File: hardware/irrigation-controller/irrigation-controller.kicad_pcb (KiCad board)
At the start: 2 copper layers, 0 parts

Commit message: Initial controller pcb footprint import
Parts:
- added C1: 100nF, Capacitor_SMD:C_0603_1608Metric, F.Cu at (190.5, 84.8)
- added C10: 15pF, Capacitor_SMD:C_0603_1608Metric, F.Cu at (259.0, 73.2)
- added C11: 8.2nF, Capacitor_SMD:C_0603_1608Metric, F.Cu at (239.0, 153.4)
- added C12: 8.2nF, Capacitor_SMD:C_0603_1608Metric, F.Cu at (260.9, 62.8)
- added C13: 2.7nF, Capacitor_SMD:C_0603_1608Metric, F.Cu at (257.6, 143.8)
- added C14: 1.5nF, Capacitor_SMD:C_0402_1005Metric, F.Cu at (263.1, 77.6)
- added C15: 100nF, Capacitor_SMD:C_0603_1608Metric, F.Cu at (253.7, 136.9)
- added C16: 100nF, Capacitor_SMD:C_0603_1608Metric, F.Cu at (256.8, 66.7)
- added C17: 10uF, Capacitor_SMD:C_1206_3216Metric, F.Cu at (242.1, 122.2)
- added C18: 10uF, Capacitor_SMD:C_1206_3216Metric, F.Cu at (271.0, 74.7)
- added C19: 10uF, Capacitor_SMD:C_1206_3216Metric, F.Cu at (227.6, 144.2)
- added C2: 100nF, Capacitor_SMD:C_0603_1608Metric, F.Cu at (174.6, 100.7)
- added C20: 10uF, Capacitor_SMD:C_1206_3216Metric, F.Cu at (253.7, 83.9)
- added C21: 10uF, Capacitor_SMD:C_1206_3216Metric, F.Cu at (236.7, 122.2)
- added C22: 10uF, Capacitor_SMD:C_1206_3216Metric, F.Cu at (261.4, 83.4)
- added C3: 100nF, Capacitor_SMD:C_0603_1608Metric, F.Cu at (149.9, 117.6)
- added C4: 100nF, Capacitor_SMD:C_0603_1608Metric, F.Cu at (145.8, 117.6)
- added C5: 22pF, Capacitor_SMD:C_0402_1005Metric, F.Cu at (182.0, 102.2)
- added C6: 22pF, Capacitor_SMD:C_0402_1005Metric, F.Cu at (167.9, 116.5)
- added C7: 10uF, Capacitor_SMD:C_1206_3216Metric, F.Cu at (221.5, 144.3)
- added C8: 10uF, Capacitor_SMD:C_1206_3216Metric, F.Cu at (250.4, 65.2)
- added C9: 27pF, Capacitor_SMD:C_0603_1608Metric, F.Cu at (250.7, 146.0)
- added D1: 1.1V 1A, Diode_SMD:D_SMA, F.Cu at (180.0, 85.9)
- added D2: 1.1V 1A, Diode_SMD:D_SMA, F.Cu at (147.9, 114.1)
- added D3: 550mV 1A, Diode_SMD:D_SMA, F.Cu at (247.7, 131.6)
- added D4: 550mV 1A, Diode_SMD:D_SMA, F.Cu at (265.1, 67.8)
- added J1: RS485, Connector_JST:JST_XH_B3B-XH-A_1x03_P2.50mm_Vertical, F.Cu at (118.7, 73.0)
- added J10: I2C_2, Connector_JST:JST_XH_B4B-XH-A_1x04_P2.50mm_Vertical, F.Cu at (97.1, 70.8)
- added J11: IO, Connector_PinHeader_2.54mm:PinHeader_2x04_P2.54mm_Vertical, F.Cu at (82.5, 84.3)
- added J12: RELAY_2, Connector_JST:JST_XH_B2B-XH-A_1x02_P2.50mm_Vertical, F.Cu at (110.9, 63.9)
- added J13: RELAY_3B, Connector_JST:JST_XH_B3B-XH-A_1x03_P2.50mm_Vertical, F.Cu at (89.8, 53.5)
- added J14: RELAY_4B, Connector_JST:JST_XH_B3B-XH-A_1x03_P2.50mm_Vertical, F.Cu at (127.7, 53.8)
- added J2: I2C_1, Connector_JST:JST_XH_B4B-XH-A_1x04_P2.50mm_Vertical, F.Cu at (97.5, 82.1)
- added J3: ATMEGA ICSP, Connector_PinHeader_2.54mm:PinHeader_2x03_P2.54mm_Vertical, F.Cu at (105.8, 51.9)
- added J4: ATMEGA UART, Connector_PinHeader_2.54mm:PinHeader_2x03_P2.54mm_Vertical, F.Cu at (111.7, 81.1)
- added J5: RF Module, Connector_PinSocket_2.54mm:PinSocket_1x07_P2.54mm_Vertical, F.Cu at (88.4, 62.2)
- added J6: PWR, Connector_JST:JST_XH_B2B-XH-A_1x02_P2.50mm_Vertical, F.Cu at (130.8, 72.7)
- added J7: RELAY_1, Connector_JST:JST_XH_B2B-XH-A_1x02_P2.50mm_Vertical, F.Cu at (195.0, 57.6)
- added J8: RELAY_3A, Connector_JST:JST_XH_B3B-XH-A_1x03_P2.50mm_Vertical, F.Cu at (125.5, 63.7)
- added J9: RELAY_4A, Connector_JST:JST_XH_B3B-XH-A_1x03_P2.50mm_Vertical, F.Cu at (115.7, 53.8)
- added K1: UA2-5NU, lib:Relay_DPDT_NEXEM_UA2_Pitch3.2mm, F.Cu at (145.1, 97.1)
- added K2: UA2-5NU, lib:Relay_DPDT_NEXEM_UA2_Pitch3.2mm, F.Cu at (170.0, 58.3)
- added L1: 4.7uH, Capacitor_THT:C_Radial_D5.0mm_H5.0mm_P2.00mm, F.Cu at (260.1, 110.5)
- added L2: 4.7uH, Capacitor_THT:C_Radial_D5.0mm_H5.0mm_P2.00mm, F.Cu at (242.5, 65.9)
- added Q1: MMBT3904, Package_TO_SOT_SMD:SOT-23, F.Cu at (167.9, 108.7)
- added Q2: MMBT3904, Package_TO_SOT_SMD:SOT-23, F.Cu at (184.8, 90.4)
- added Q3: 2N7002, Package_TO_SOT_SMD:SOT-23, F.Cu at (186.3, 85.9)
- added Q4: 2N7002, Package_TO_SOT_SMD:SOT-23, F.Cu at (177.6, 97.2)
- added Q5: 2N7002, Package_TO_SOT_SMD:SOT-23, F.Cu at (162.3, 112.1)
- added Q6: 2N7002, Package_TO_SOT_SMD:SOT-23, F.Cu at (170.3, 101.7)
- added R1: 2.2k, Resistor_SMD:R_0402_1005Metric, F.Cu at (129.0, 109.0)
- added R10: 10k, Resistor_SMD:R_0402_1005Metric, F.Cu at (133.3, 87.2)
- added R11: 10k, Resistor_SMD:R_0402_1005Metric, F.Cu at (185.2, 95.7)
- added R12: 120, Resistor_SMD:R_0603_1608Metric, F.Cu at (189.0, 89.9)
- added R13: 10k, Resistor_SMD:R_0402_1005Metric, F.Cu at (175.6, 107.4)
- added R14: 10k, Resistor_SMD:R_0402_1005Metric, F.Cu at (167.9, 114.5)
- added R15: 10k, Resistor_SMD:R_0402_1005Metric, F.Cu at (184.1, 98.2)
- added R16: 10k, Resistor_SMD:R_0402_1005Metric, F.Cu at (265.2, 149.4)
- added R17: 3k, Resistor_SMD:R_0603_1608Metric, F.Cu at (264.9, 144.3)
- added R18: 10k, Resistor_SMD:R_0402_1005Metric, F.Cu at (240.6, 74.4)
- added R19: 1.8k, Resistor_SMD:R_0603_1608Metric, F.Cu at (245.2, 78.4)
- added R2: 620, Resistor_SMD:R_0603_1608Metric, F.Cu at (166.5, 112.3)
- added R20: 10k, Resistor_SMD:R_0402_1005Metric, F.Cu at (170.0, 112.0)
- added R3: 620, Resistor_SMD:R_0603_1608Metric, F.Cu at (181.8, 95.9)
- added R4: 2.2k, Resistor_SMD:R_0402_1005Metric, F.Cu at (162.8, 117.9)
- added R5: 10k, Resistor_SMD:R_0402_1005Metric, F.Cu at (181.2, 98.2)
- added R6: 10k, Resistor_SMD:R_0402_1005Metric, F.Cu at (159.9, 117.9)
- added R7: 10k, Resistor_SMD:R_0402_1005Metric, F.Cu at (184.0, 93.7)
- added R8: 12k, Resistor_SMD:R_0603_1608Metric, F.Cu at (252.2, 150.4)
- added R9: 20k, Resistor_SMD:R_0603_1608Metric, F.Cu at (256.4, 78.7)
- added SW1: SPST, lib:SW_SPST_THT_5.0mm, F.Cu at (183.1, 58.3)
- added U1: AQY280EH, Package_DIP:DIP-4_W7.62mm, F.Cu at (157.3, 89.2)
- added U2: ATmega328P-AU, Package_QFP:TQFP-32_7x7mm_P0.8mm, F.Cu at (101.0, 108.5)
- added U3: AQY280EH, Package_DIP:DIP-4_W7.62mm, F.Cu at (125.2, 112.7)
- added U4: TPS54331DR, TPS54331DR:Texas_Instruments-TPS54331DR-Level_A, F.Cu at (242.3, 145.8)
- added U5: TPS54331DR, TPS54331DR:Texas_Instruments-TPS54331DR-Level_A, F.Cu at (249.8, 72.4)
- added U6: MAX485, Package_DIP:DIP-8_W7.62mm, F.Cu at (146.5, 85.4)
- added Y1: 8MHz, Crystal:Crystal_SMD_5032-2Pin_5.0x3.2mm, F.Cu at (127.2, 105.6)
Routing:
- added copper zone on B.Cu, net GND
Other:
- board outline added: 207.8 x 117.3 mm

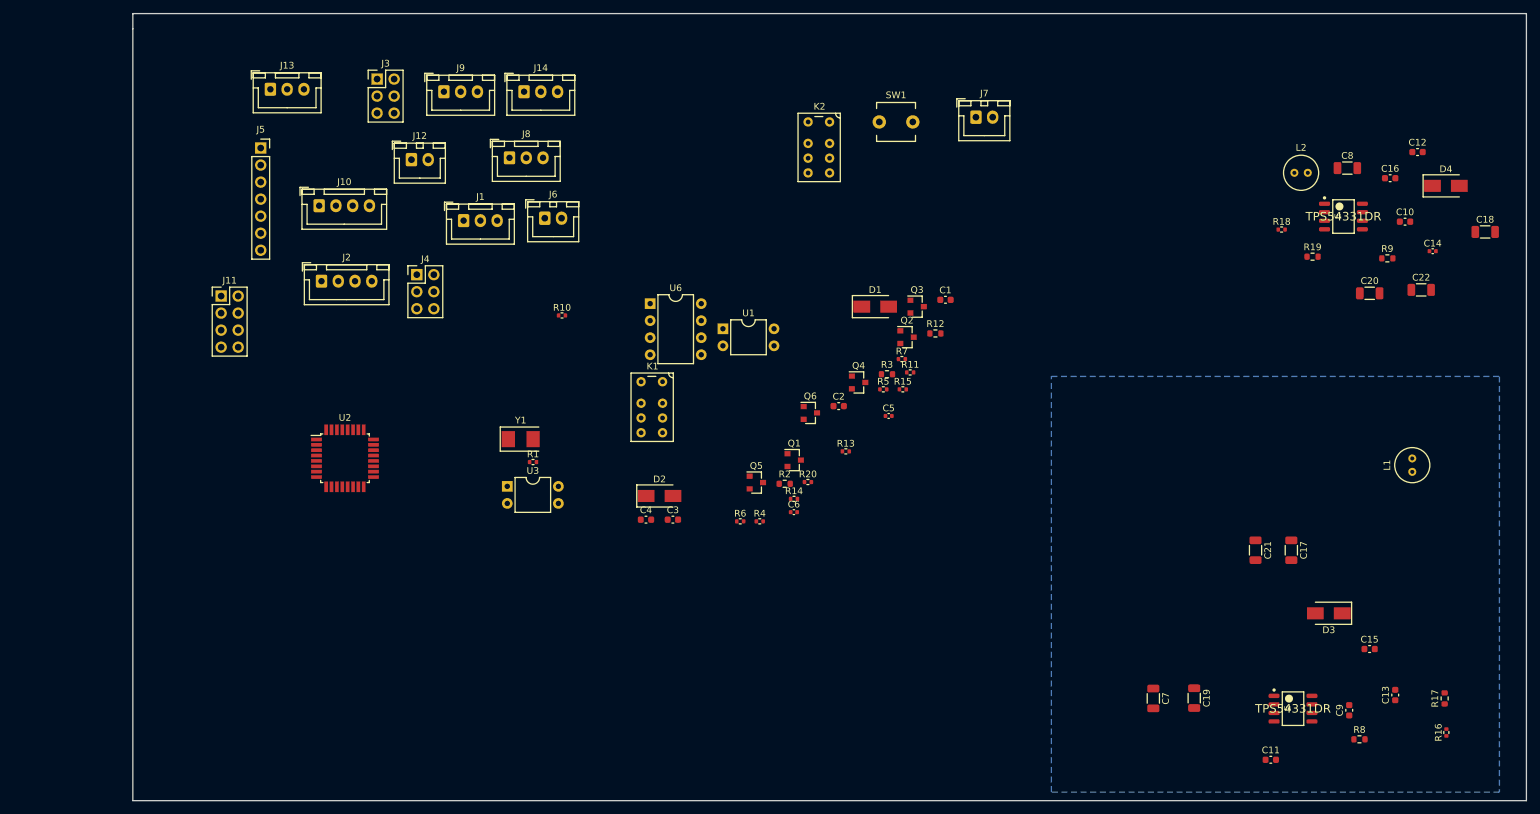
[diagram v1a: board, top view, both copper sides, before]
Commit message: Controller board layout wip
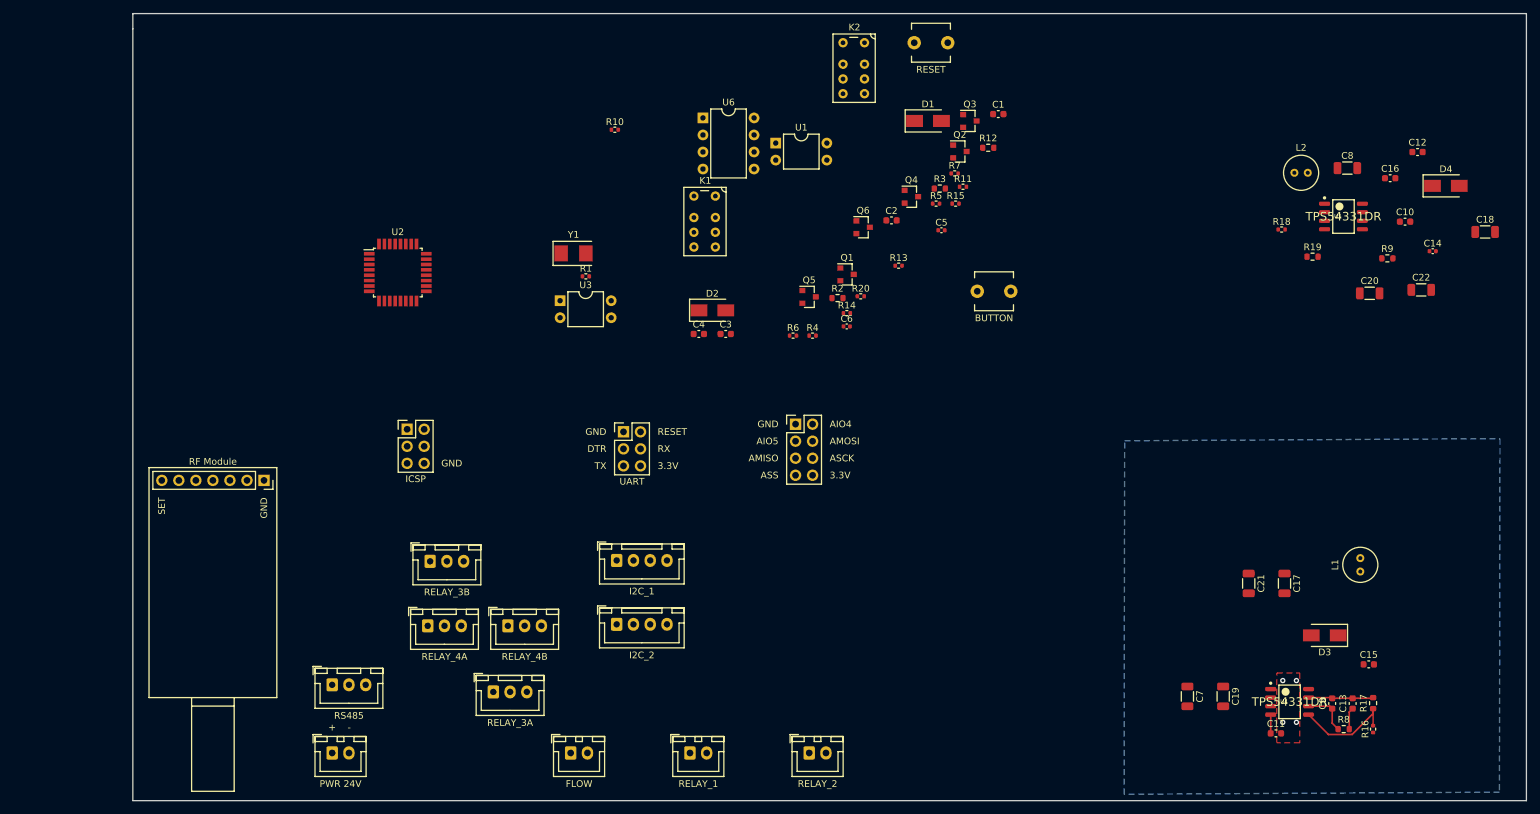
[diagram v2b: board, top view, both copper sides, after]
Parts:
- added J15: FLOW, Connector_JST:JST_XH_B2B-XH-A_1x02_P2.50mm_Vertical, F.Cu at (134.6, 152.4)
- added SW2: BUTTON, lib:SW_SPST_THT_5.0mm, F.Cu at (197.7, 83.6)
- J3: value ATMEGA ICSP -> ICSP
- J4: value ATMEGA UART -> UART
- J6: value PWR -> PWR 24V
- SW1: value SPST -> RESET
- moved J12 106.5 mm to (170.2, 152.4)
- moved J7 103.9 mm to (152.4, 152.4)
- moved J11 87.7 mm to (168.1, 103.4)
- moved J6 85.8 mm to (99.1, 152.4)
- moved J8 79.7 mm to (123.1, 143.3)
- moved J14 79.7 mm to (125.3, 133.4)
- moved J9 79.7 mm to (113.3, 133.4)
- moved J10 76.6 mm to (141.5, 133.2)
- moved J13 74.3 mm to (113.7, 123.8)
- moved J1 71.9 mm to (99.1, 142.2)
- moved J2 60.6 mm to (141.5, 123.7)
- moved J3 52.4 mm to (110.2, 104.1)
- moved J5 49.6 mm to (88.9, 111.8), turned to 270 degrees
- moved J4 38.7 mm to (142.5, 104.5)
- moved Q1 28.8 mm to (175.8, 81.0)
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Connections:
- J3 pad 1: GND -> AMISO
- J3 pad 2: ARESET -> +3V3
- J3 pad 4: AMISO -> AMOSI
- J3 pad 5: AMOSI -> ARESET
- J3 pad 6: +3V3 -> GND
- U2 pad 1: ASRX -> AIO5
- U2 pad 12: AIO2 -> ASTX
- U2 pad 13: AIO3 -> ASRX
- U2 pad 2: AIO1 -> AIO2
- U2 pad 24: AIO5 -> AIO3
- U2 pad 9: ASTX -> AIO1
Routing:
- net Net-(R16-Pad2): track 0.00 -> 15.4 mm
- net GND: track 0.00 -> 9.70 mm, vias 0 -> 4
- net Net-(C9-Pad1): track 0.00 -> 7.10 mm
- net Net-(C13-Pad1): track 0.00 -> 3.26 mm
- net Net-(C11-Pad1): track 0.00 -> 2.80 mm
- added copper zone on F.Cu, net GND

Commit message: Controller pcb layout mostly complete
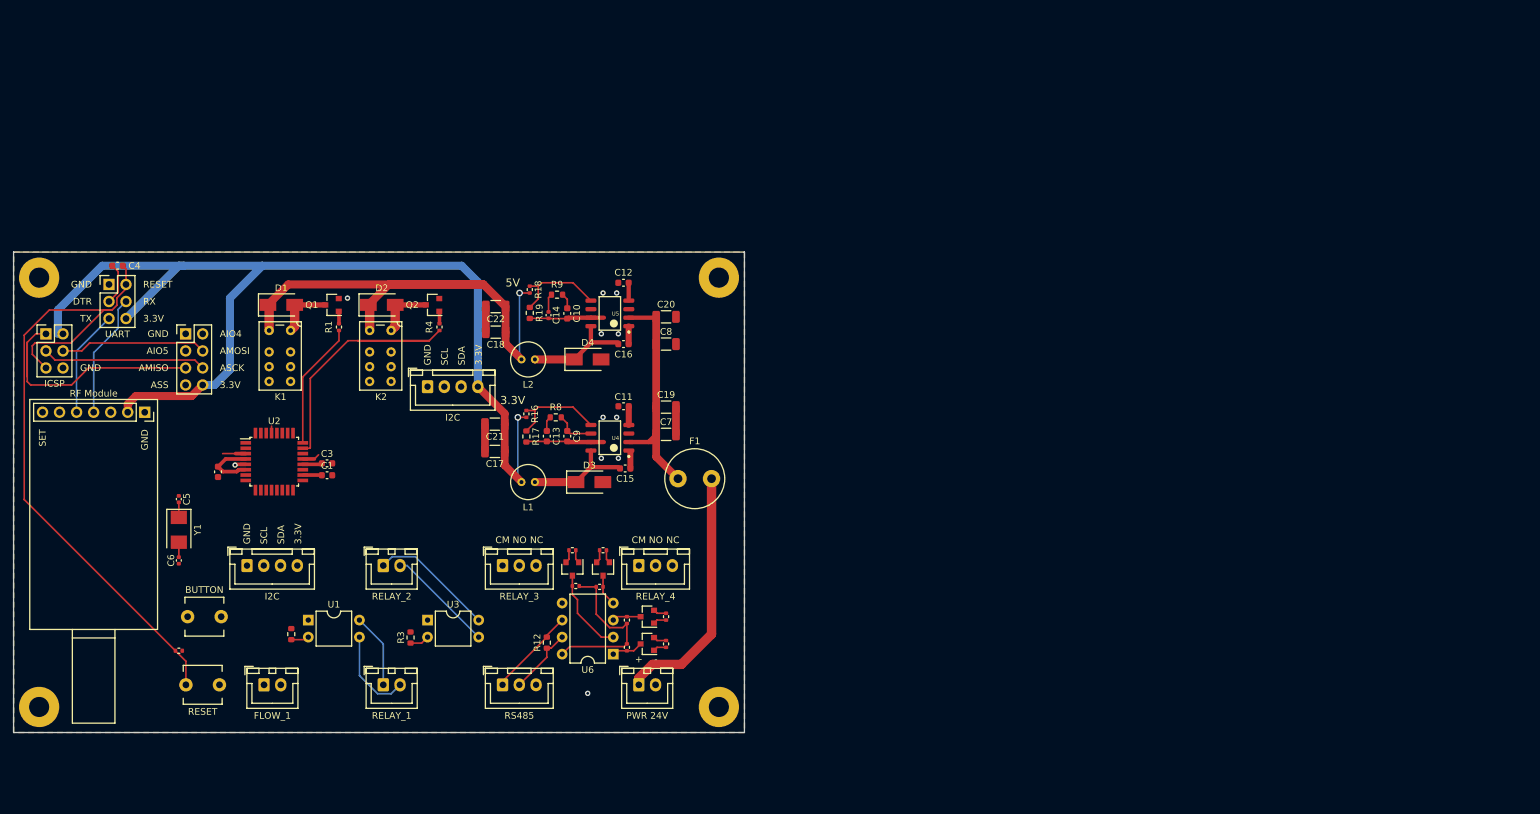
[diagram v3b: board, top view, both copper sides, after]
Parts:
- removed J13: RELAY_3B, Connector_JST:JST_XH_B3B-XH-A_1x03_P2.50mm_Vertical
- removed J14: RELAY_4B, Connector_JST:JST_XH_B3B-XH-A_1x03_P2.50mm_Vertical
- added F1: Fuse, Inductor_THT:L_Radial_D8.7mm_P5.00mm_Fastron_07HCP, F.Cu at (150.6, 111.5)
- added H1: MountingHole_Pad, MountingHole:MountingHole_3mm_Pad, F.Cu at (55.4, 81.5)
- added H2: MountingHole_Pad, MountingHole:MountingHole_3mm_Pad, F.Cu at (55.4, 145.5)
- added H3: MountingHole_Pad, MountingHole:MountingHole_3mm_Pad, F.Cu at (156.7, 81.5)
- added H4: MountingHole_Pad, MountingHole:MountingHole_3mm_Pad, F.Cu at (156.7, 145.5)
- J10: value I2C_2 -> I2C
- J15: value FLOW -> FLOW_1
- J2: value I2C_1 -> I2C
- J8: value RELAY_3A -> RELAY_3
- J9: value RELAY_4A -> RELAY_4
- K1: value UA2-5NU -> RELAY_3
- K2: value UA2-5NU -> RELAY_4
- moved C18 148.3 mm to (123.4, 89.7), turned to 180 degrees
- moved SW1 144.8 mm to (79.8, 142.2)
- moved C22 138.0 mm to (123.4, 85.9), turned to 180 degrees
- moved R16 134.7 mm to (128.0, 101.9)
- moved R17 132.3 mm to (128.0, 105.2), turned to 270 degrees
- moved C14 132.2 mm to (131.3, 87.1), turned to 270 degrees
- moved R5 131.1 mm to (76.2, 137.2), turned to 180 degrees
- moved D4 130.5 mm to (137.2, 93.7)
- moved SW2 127.3 mm to (80.0, 132.1), turned to 180 degrees
- moved C13 126.6 mm to (131.1, 105.2), turned to 270 degrees
- moved R8 126.3 mm to (132.4, 102.4), turned to 180 degrees
- moved C10 125.7 mm to (134.1, 86.9), turned to 270 degrees
- moved R9 123.9 mm to (132.6, 84.1), turned to 180 degrees
- moved L1 123.8 mm to (129.3, 112.0), turned to 180 degrees
- moved C9 120.8 mm to (134.1, 105.2), turned to 270 degrees
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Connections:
- J4 pad 4: ARXD -> ATXD
- J4 pad 5: ATXD -> ARXD
- J6 pad 1: +24V -> Net-(F1-Pad2)
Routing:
- net +3V3: track 0.00 -> 182.0 mm, vias 0 -> 1
- net +5V: track 0.00 -> 110.3 mm, vias 0 -> 1
- net ARESET: track 0.00 -> 103.5 mm
- net AIO4: track 0.00 -> 44.4 mm
- net AMISO: track 0.00 -> 39.1 mm
- net Net-(F1-Pad2): track 0.00 -> 38.0 mm
- net +24V: track 0.00 -> 35.0 mm
- net GND: track 9.70 -> 42.4 mm, vias 4 -> 11
- net ASCK: track 0.00 -> 24.4 mm
- net AMOSI: track 0.00 -> 21.8 mm
- net AIO3: track 0.00 -> 19.0 mm
- net R2A: track 0.00 -> 18.7 mm
- net ATXD: track 0.00 -> 18.5 mm
- net Net-(C15-Pad1): track 0.00 -> 16.2 mm
- net R2B: track 0.00 -> 16.1 mm
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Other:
- board size 207.8 x 117.3 mm -> 109 x 71.6 mm
- board text added: "3.3V"
- board text added: "5V"
